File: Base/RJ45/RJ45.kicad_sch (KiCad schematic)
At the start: 36 parts, among them J1 Barrel_Jack_Switch, J2 AudioJack2_Ground, J3 AudioJack2_Ground, J4 RJ45, U2 OPA1656

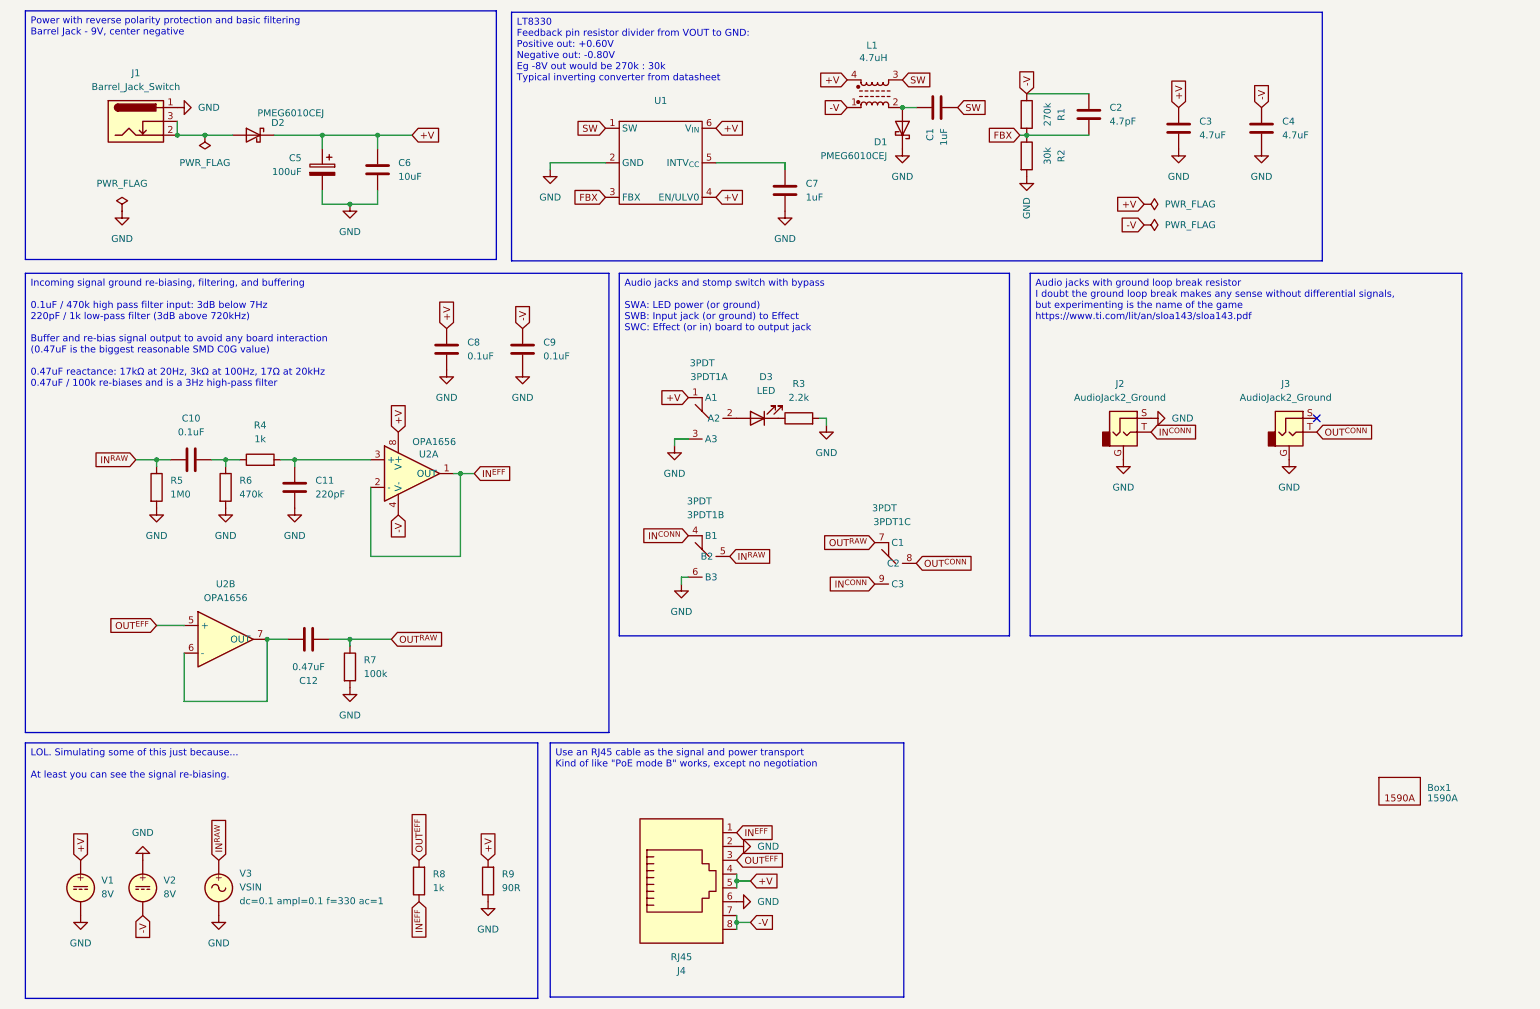
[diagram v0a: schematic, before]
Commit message: Switch to a shielded RJ45 connector for the RJ45 test boards
It turns out that all my ethernet cables I had around look to be plain
unshielded twisted pairs (UTP), and some very preliminary testing shows
that they are very noisy and I'd need to use differential signalling to
make the whole "connect the base and effect with an ethernet cable"
scheme work.

I know, I know, that's technically the right thing to do anyway, but I
really don't think it's an option.  It adds way too much effort at the
effects end, at that point I'm better off just keeping the two together.

Even if some of my recent circuits have been differential (ie that whole
multiplier thing), I don't want to force that on everything.

And yes, the ethernet cable idea might have been a stupid idea and any
first-year EE would probably have told me that.  I'm a SW guy, remember?

But before giving up, let's just try the single-ended model with proper
shielded cables and shielded connectors.  The double-shielded cables are
a thing, with each twisted pair foil-shielded and then the whole cable
having a braided shield.

That would seem to be no worse than a normal 1/4" audio cable, even if
the same cable also carries power.  I'm looking for a few feet, not long
runs.  Knock wood.

And the shielding is part of the CAT8 specs, so this is standard cable
these days and cheap, even if my random box of cables was full of the
old crappy stuff of yesteryear.

So maybe this model is still salvageable with single-ended signaling.
Because I'd love to separate the stomp switch and audio jacks from the
actual effect side.

Signed-off-by: Linus Torvalds <torvalds@linux-foundation.org>
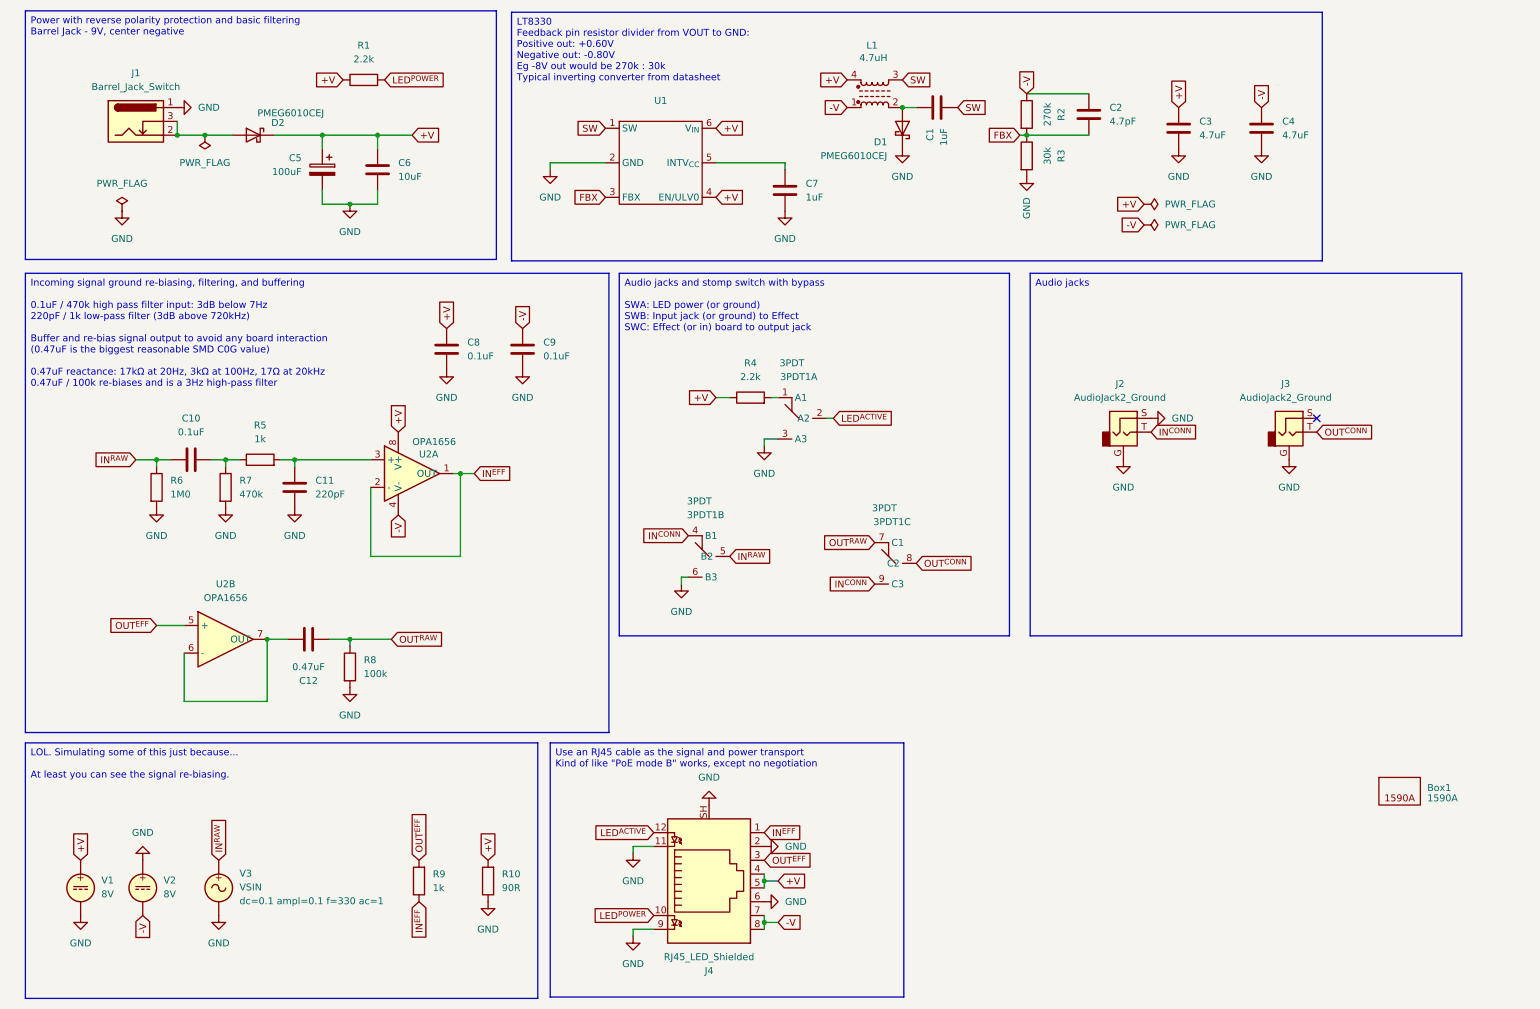
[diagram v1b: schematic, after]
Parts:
- removed D3: LED, Mylib:Würth Reverse Mount LED, symbol Device:LED
- removed J4: RJ45, Connector_RJ:RJ45_OST_PJ012-8P8CX_Vertical, symbol Connector:RJ45
- added J4: RJ45_LED_Shielded, Connector_RJ:RJ45_Amphenol_RJHSE538X, symbol Connector:RJ45_LED_Shielded
- added R1: 2.2k, Resistor_SMD:R_0805_2012Metric_Pad1.20x1.40mm_HandSolder, symbol Device:R
- renumbered R9 to R10, R1 to R2, R2 to R3, R3 to R4, R4 to R5, R5 to R6, R6 to R7, R7 to R8, R8 to R9
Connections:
- net +V: now also R4.1, J4.4, J4.5, R1.1; no longer 3PDT1.1 (A1)
- net -V: now also J4.7, J4.8
- net GND: now also J4.11, J4.2, J4.6, J4.9, J4.SH; no longer R4.2
- net IN^{EFF}: now also J4.1
- net OUT^{EFF}: now also J4.3
- net LED^{ACTIVE}: now reaches 3PDT1.2 (A2)
- net LED^{ACTIVE}: now also J4.12
- new net: 3PDT1.1 (A1), R4.2
- new net LED^{POWER}: J4.10, R1.2
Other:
- moved on the sheet: 3PDT1A, R4

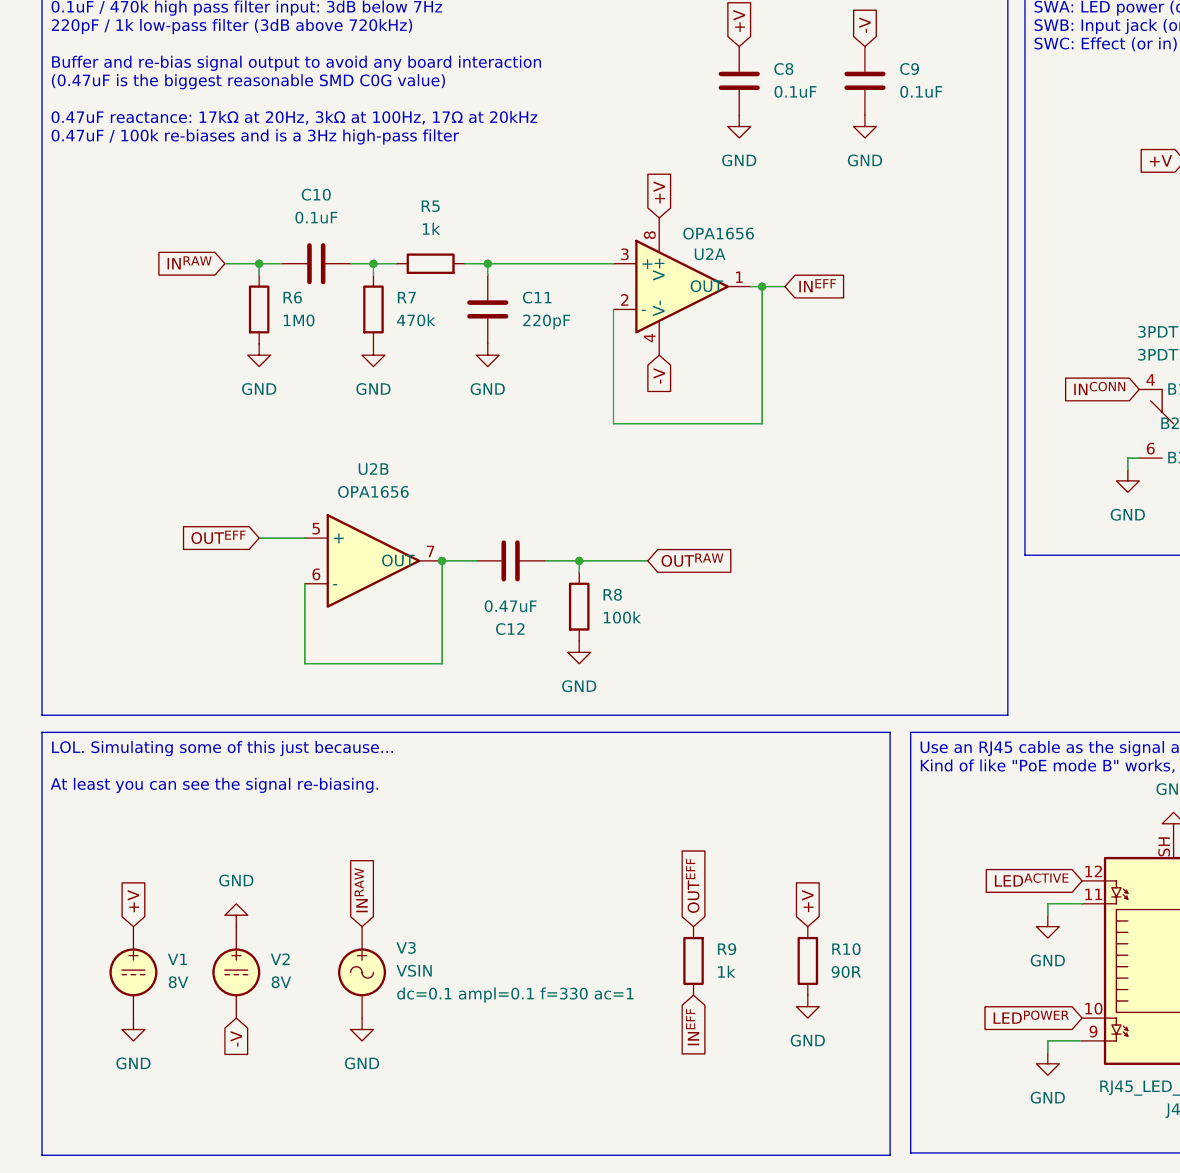
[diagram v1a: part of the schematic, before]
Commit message: RJ45: hopefully make the base board actually work
Ok, with some boards back and populated, that whole "feed signal over
RJ45" didn't work at all.  I still think the concept should work, but my
implementation of it is obviously very broken.

The op amp output to the effect ends up oscillating wildly at a
frequency of a few MHz.  And while I might have screwed something else
up, I think it's because of a capacitive load in the form of that cable.

According to random searches I did, the minimal fix is typically to add
a small resistive load in series on the output.  So I did that.

But thinking about it, the other end is very possibly going to have the
same problem, and none of the existing effects boards were designed with
any of this in mind.

So I will also be updating the test board at the other end of the cable
to do active buffering and I suspect I really should rebias the signal
too at that point so that the existing effects boards see the
traditional VGND setup instead of the quick hack that just passively
changed the rules under them.

It may obviously still be the case that this is all just misguided
garbage, but before throwing it in the bin, let's try to do it right.
That includes adding some transmission line simulation, even if that
didn't actually show the issue (with or without the series resistor).

Maybe it's something else entirely that I'm not seeing / understanding.

Signed-off-by: Linus Torvalds <torvalds@linux-foundation.org>
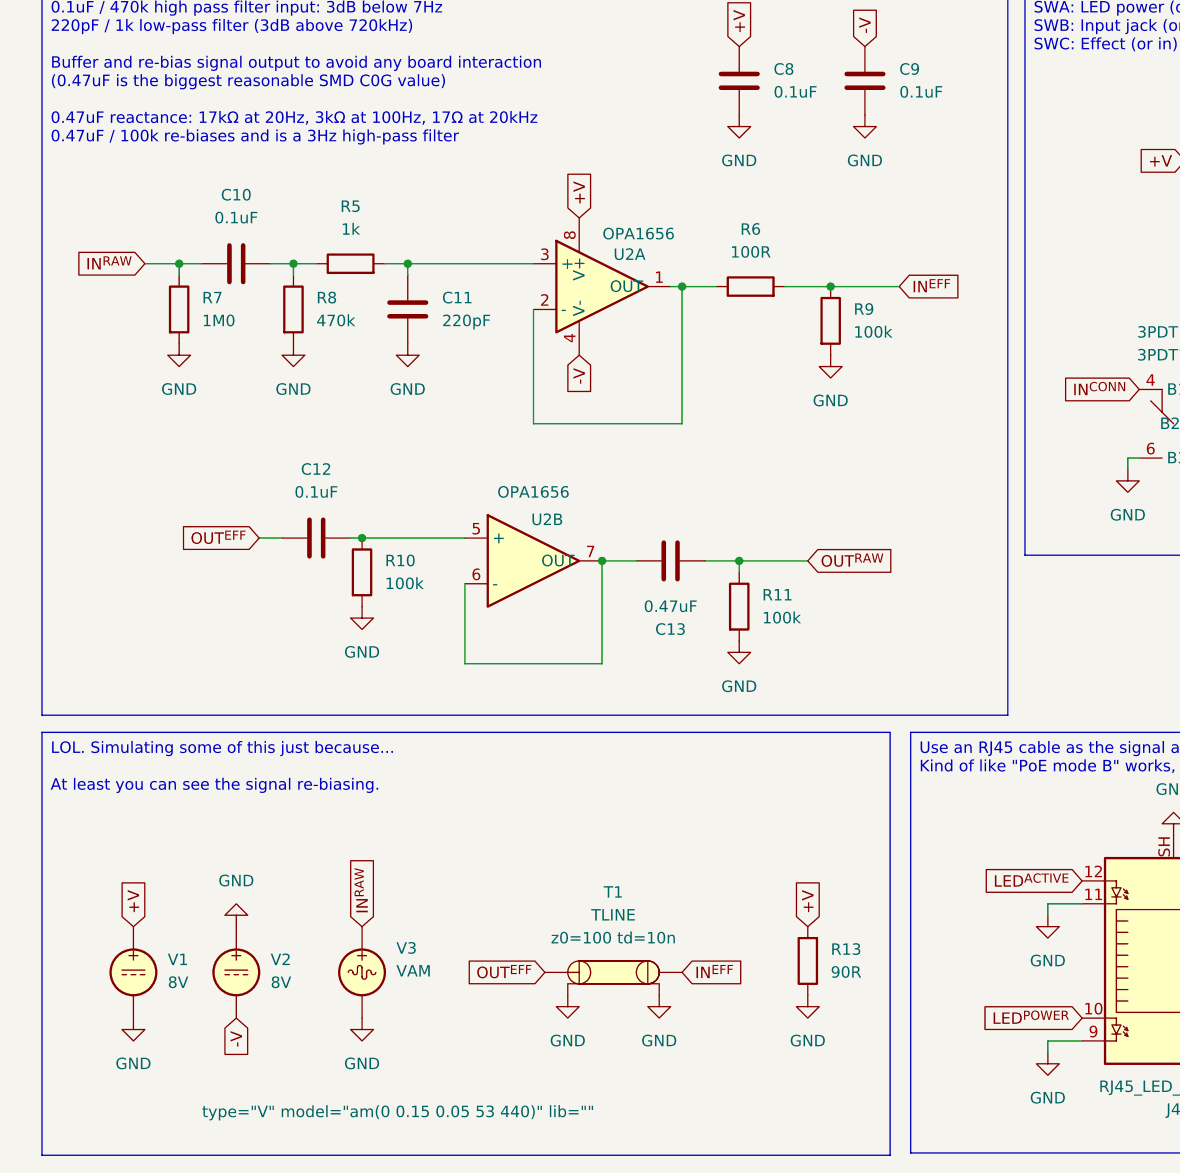
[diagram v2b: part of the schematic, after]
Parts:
- removed V3: VSIN, symbol Simulation_SPICE:VSIN
- added C12: 0.1uF, Mylib:C_0704_1810Metric, symbol Device:C
- added R10: 100k, Resistor_SMD:R_0805_2012Metric_Pad1.20x1.40mm_HandSolder, symbol Device:R
- added R6: 100R, Resistor_SMD:R_0805_2012Metric_Pad1.20x1.40mm_HandSolder, symbol Device:R
- added T1: TLINE, symbol Simulation_SPICE:TLINE
- added V3: VAM, symbol Simulation_SPICE:VAM
- R9: value 1k -> 100k; footprint (none) -> Resistor_SMD:R_0805_2012Metric_Pad1.20x1.40mm_HandSolder; now in the parts list
- renumbered C12 to C13, R8 to R11, R10 to R13, R6 to R7, R7 to R8
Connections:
- net GND: now also R9.2, R10.2, T1.2, T1.4, V3.2
- net IN^{EFF}: now also R6.2, T1.3; no longer U2.1 (OUT), U2.2 (-)
- net IN^{RAW}: now also V3.1
- net OUT^{EFF}: now also C12.1, T1.1; no longer R9.2, U2.5 (+)
- new net: C12.2, R10.1, U2.5 (+)
- new net: R6.1, U2.1 (OUT), U2.2 (-)
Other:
- moved on the sheet: C10, C11, C13, R11, R5, R7, R8, U2A, U2B
